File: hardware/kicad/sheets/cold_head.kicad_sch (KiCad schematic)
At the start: 13 parts, among them J12 RTD PT1000 4-wire, U22 ADS122C04IPWR

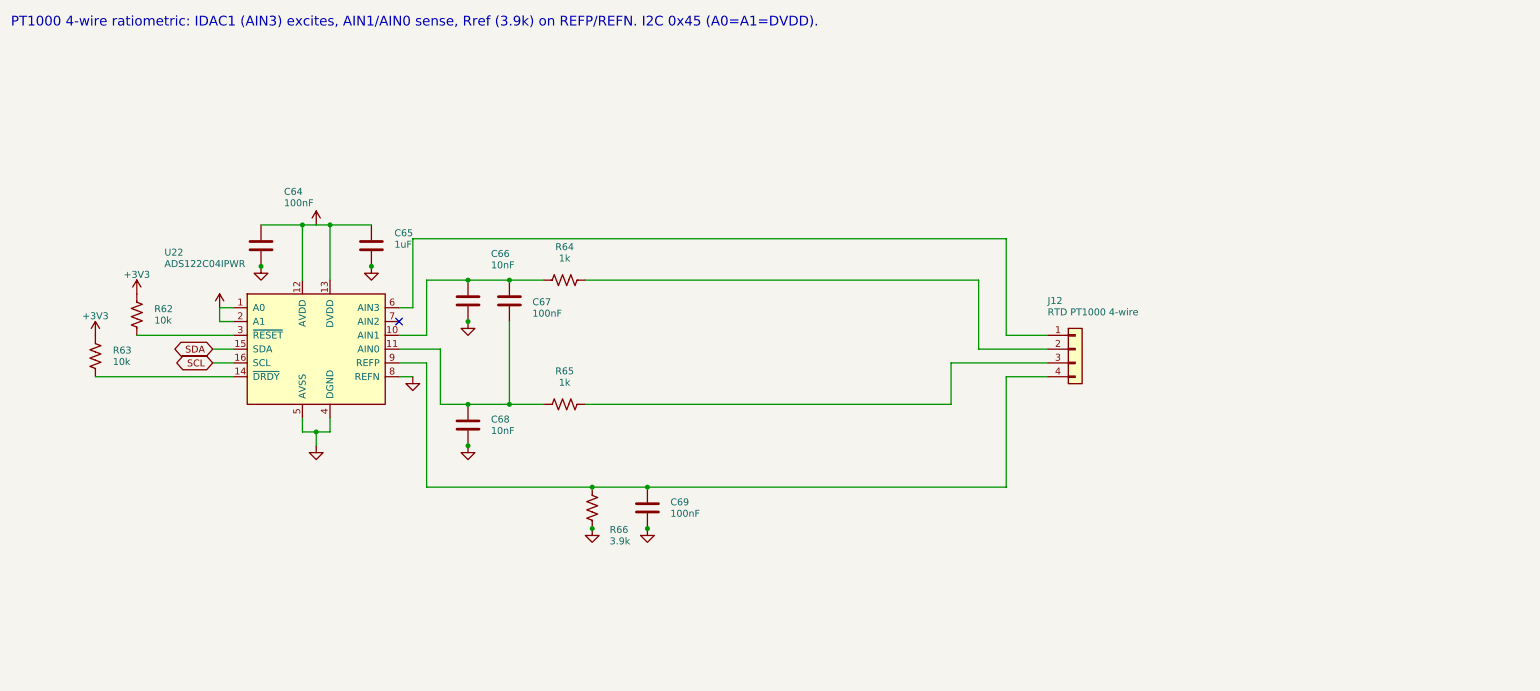
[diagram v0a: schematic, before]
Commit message: KiCad: cleaner layout, decoupling blocks, label directions, KiCad format fixes
- move IC decoupling caps into labelled blocks at the side of each sheet
- global labels show input/output direction per net
- no 4-way junctions (generator now checks and fails)
- generator output matches KiCad's saved format (hide property, junction
  and wire normalisation, lib symbol embedded fonts, multi-unit pins)
- hand-laid USB ESD protection as a pass-through

Co-Authored-By: Claude Sonnet 5.5 <noreply@anthropic.com>
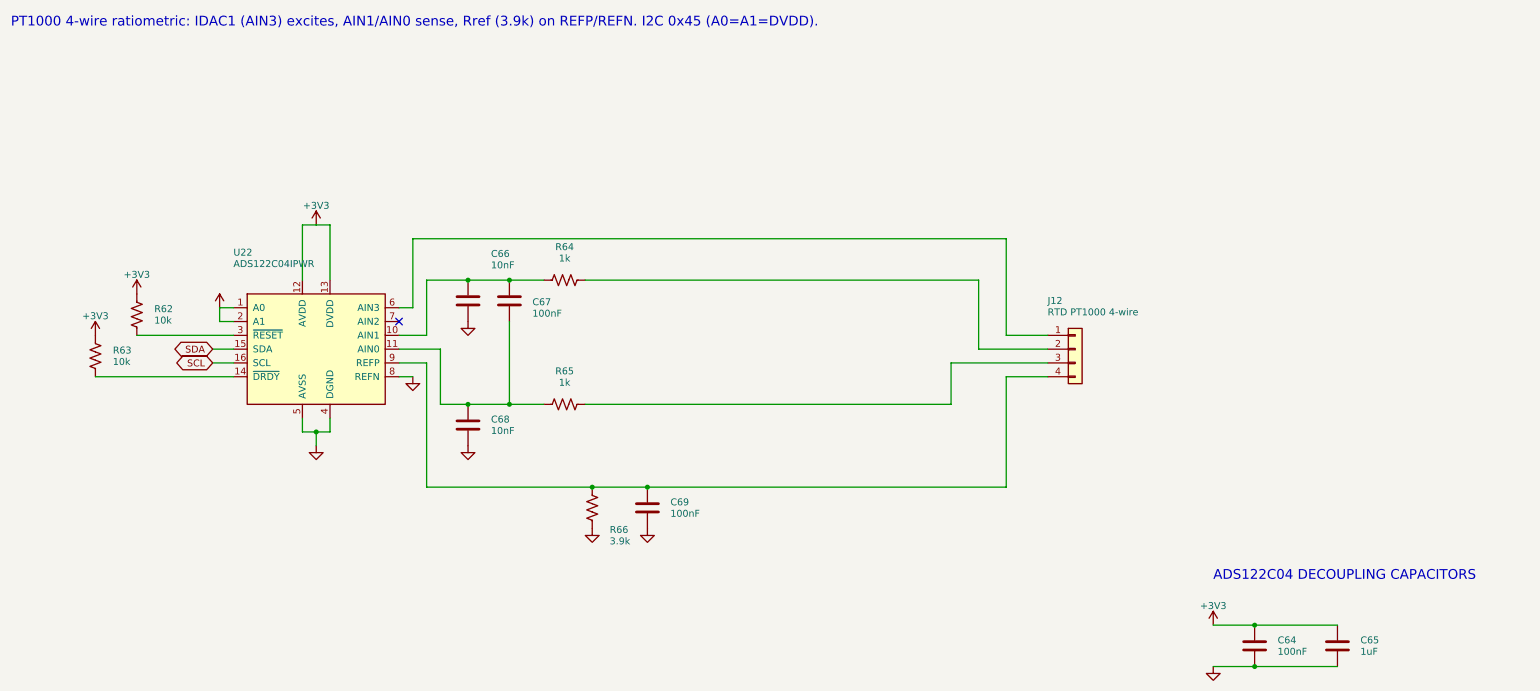
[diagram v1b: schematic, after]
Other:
- note added: "ADS122C04 DECOUPLING CAPACITORS"
